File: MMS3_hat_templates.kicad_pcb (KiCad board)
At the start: 4 copper layers, 100 x 50 mm, 61 parts, among them J1 Chainbus in, J2 Chainbus Out, J3 Conn_01x04_Pin, J4 AMASS XT60 Male, J5 AMASS XT60 Female, J8 Conn_01x03_Pin, SW1 SW_DIP_x04, U2 M24C64, U3 SN74CB3Q3245PWR, U4 AMS1117, U5 LM2596HVS-ADJRG

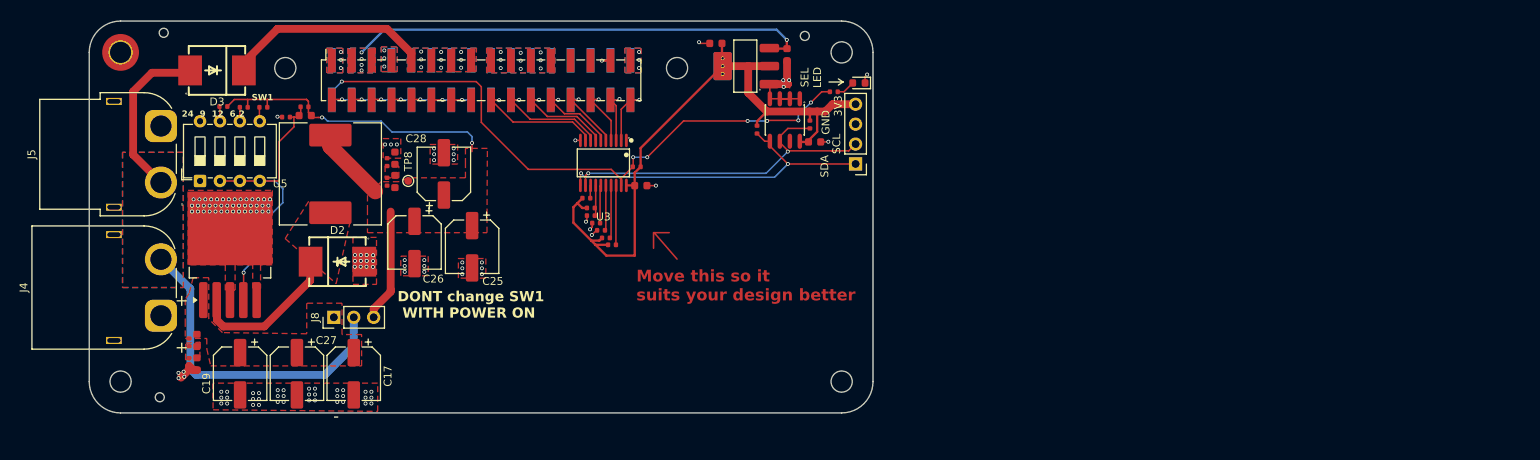
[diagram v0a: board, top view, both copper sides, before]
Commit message: ServoController
Dodano arkusz sterownika servo, aktualizacja polaczen
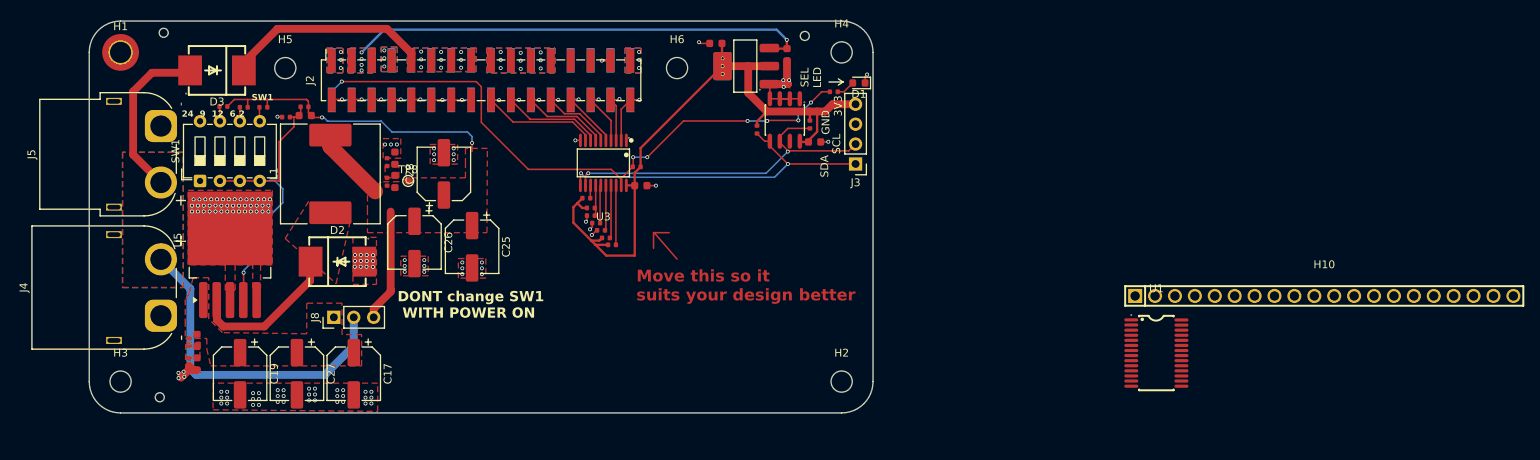
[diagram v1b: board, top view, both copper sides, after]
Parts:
- added H10: 210S-1*20P L=11.6MMGold-plated black, easyeda2kicad:HDR-TH_20P-P2.54-V-M-1, F.Cu at (235.6, 123.1)
- added U1: PCA9685PW,118, easyeda2kicad:TSSOP-28_L9.7-W4.4-P0.65-LS6.4-TL, F.Cu at (214.2, 130.4)

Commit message: updated PCB to up-to-date template:
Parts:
- removed C16, C18: 10uF, PCM_JLCPCB:C_0603
- removed C17, C19, C25, C26, C27, C28: 47u, Capacitor_SMD:CP_Elec_6.3x7.7
- removed C2, C20, C21, C23, C24: 100nF, PCM_JLCPCB:C_0603
- removed C22: 3.3nF, PCM_JLCPCB:C_0603
- removed D1: LED, LED_SMD:LED_0603_1608Metric
- removed D2, D3: SS510C, SS510C:SMC_L7.1-W6.2-LS8.1-RD
- removed H10: 210S-1*20P L=11.6MMGold-plated black, easyeda2kicad:HDR-TH_20P-P2.54-V-M-1
- removed H7, H8, H9: ~, PCM_JLCPCB:Hole_Tooling_JLCPCB
- removed L1: 100uH 4A, Inductor_SMD:L_Sunlord_SWRB1207S
- removed R12: 1kΩ, PCM_JLCPCB:R_0402
- removed R13: 18.7k, PCM_JLCPCB:R_0402
- removed R14: 16.5k, PCM_JLCPCB:R_0402
- removed R15: 9.53k, PCM_JLCPCB:R_0402
- removed R16: 5.11k, PCM_JLCPCB:R_0402
- removed R17, R18: 33kΩ, PCM_JLCPCB:R_0402
- removed R4: 10kΩ, PCM_JLCPCB:R_0402
- removed SW1: SW_DIP_x04, Button_Switch_THT:SW_DIP_SPSTx04_Slide_6.7x11.72mm_W7.62mm_P2.54mm_LowProfile
- removed TP8: TestPoint, TestPoint:TestPoint_Pad_D1.0mm
- removed U2: M24C64, PCM_JLCPCB:SOIC-8_L5.0-W4.0-P1.27-LS6.0-BL
- removed U4: AMS1117, PCM_JLCPCB:SOT-223-3_L6.5-W3.4-P2.30-LS7.0-BR
- removed U5: LM2596HVS-ADJRG, Package_TO_SOT_SMD:TO-263-5_TabPin3
- added C29: 10uF, PCM_JLCPCB:C_0603, F.Cu at (223.5, 120.6)
- added C30: 100nF, PCM_JLCPCB:C_0603, F.Cu at (223.5, 122.9)
- added D4: SS510C, SS510C:SMC_L7.1-W6.2-LS8.1-RD, F.Cu at (100.0, 101.0)
- added D5: Red, PCM_JLCPCB:D_0603, F.Cu at (176.1, 97.9)
- added D6: Red, PCM_JLCPCB:D_0603, F.Cu at (219.6, 120.8)
- added D7: Red, PCM_JLCPCB:D_0603, F.Cu at (219.6, 123.4)
- added J10: Conn_01x03, Connector_JST:JST_XH_S3B-XH-A_1x03_P2.50mm_Horizontal, F.Cu at (140.0, 132.7)
- added J11: Conn_01x03, Connector_JST:JST_XH_S3B-XH-A_1x03_P2.50mm_Horizontal, F.Cu at (161.7, 132.7)
- added J6: Conn_01x03, Connector_JST:JST_XH_S3B-XH-A_1x03_P2.50mm_Horizontal, F.Cu at (92.2, 132.7)
- added J7: Conn_01x03, Connector_JST:JST_XH_S3B-XH-A_1x03_P2.50mm_Horizontal, F.Cu at (104.2, 132.7)
- added J9: Conn_01x03, Connector_JST:JST_XH_S3B-XH-A_1x03_P2.50mm_Horizontal, F.Cu at (128.1, 132.7)
- added R21: 10kΩ, PCM_JLCPCB:R_0402, F.Cu at (200.7, 112.8)
- added R23: 10kΩ, PCM_JLCPCB:R_0402, F.Cu at (210.4, 124.1)
- added R24: 10kΩ, PCM_JLCPCB:R_0402, F.Cu at (210.4, 126.0)
- added R25: 10kΩ, PCM_JLCPCB:R_0402, F.Cu at (210.4, 127.8)
- added R26: 10kΩ, PCM_JLCPCB:R_0402, F.Cu at (213.2, 120.4)
- added R27: 10kΩ, PCM_JLCPCB:R_0402, F.Cu at (213.2, 122.3)
- added R28: 10kΩ, PCM_JLCPCB:R_0402, F.Cu at (213.2, 124.1)
- added R29: 10kΩ, PCM_JLCPCB:R_0402, F.Cu at (213.2, 126.0)
- added R30: 10kΩ, PCM_JLCPCB:R_0402, F.Cu at (213.2, 127.8)
- added R31: 10kΩ, PCM_JLCPCB:R_0402, F.Cu at (216.1, 120.4)
- added R32: 10kΩ, PCM_JLCPCB:R_0402, F.Cu at (216.1, 122.3)
- added R33: 10kΩ, PCM_JLCPCB:R_0402, F.Cu at (216.1, 124.1)
- added R34: 10kΩ, PCM_JLCPCB:R_0402, F.Cu at (216.1, 126.0)
- J8: value Conn_01x03_Pin -> Conn_01x03; footprint Connector_PinHeader_2.54mm:PinHeader_1x03_P2.54mm_Vertical -> Connector_JST:JST_XH_S3B-XH-A_1x03_P2.50mm_Horizontal
- R10, R11: value 33kΩ -> 510Ω
- moved R11 120.0 mm to (210.4, 122.3), turned to 0 degrees
- moved R10 120.0 mm to (210.4, 120.4), turned to 0 degrees
- moved U3 63.0 mm to (206.5, 108.7), turned to 0 degrees
- moved C1 60.0 mm to (208.2, 114.0)
- moved R8 59.1 mm to (200.7, 105.4)
- moved R9 59.0 mm to (200.7, 107.2), turned to 0 degrees
- moved R20 58.1 mm to (200.7, 110.9), turned to 0 degrees
- moved R19 57.7 mm to (200.7, 109.1), turned to 0 degrees
- moved R7 56.6 mm to (197.9, 114.6)
- moved R6 54.0 mm to (197.9, 112.8)
- moved R5 53.5 mm to (197.9, 110.9)
- moved R3 35.4 mm to (197.9, 109.1), turned to 0 degrees
- moved R2 28.6 mm to (197.9, 107.2), turned to 0 degrees
- moved U1 21.0 mm to (195.1, 121.6)
- moved J4 17.1 mm to (90.5, 108.8)
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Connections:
- J4 pad 2: Vin -> /Power Connector/VIN_BRD
- J5 pad 2: Vin -> /Power Connector/VIN_BRD
- J8 pad 1: Net-(J8-Pin_1) -> GND
- J8 pad 2: Vin -> /Servo controller/S3
- J8 pad 3: U_reg -> /Power Connector/VIN_BRD
- R10 pad 1: Net-(J8-Pin_1) -> /Servo controller/S16
- R10 pad 2: Net-(C20-Pad2) -> Net-(D7-Pad2)
- R11 pad 1: Net-(C20-Pad2) -> /Servo controller/S15
- R11 pad 2: GND -> Net-(D6-Pad2)
- R19 pad 1: /Bus_switch/Chainbus.MISO -> +3V3
- R19 pad 2: GND -> /Bus_switch/Chainbus.SDA
- R2 pad 2: /Bus_switch/Chainbus.SCL -> /Bus_switch/Chainbus.CS
- R3 pad 2: /Bus_switch/Chainbus.SDA -> /Bus_switch/Chainbus.SCK
- R5 pad 1: +3V3 -> /Bus_switch/Chainbus.SCK
- R5 pad 2: /Bus_switch/Chainbus.RX -> GND
- R6 pad 2: /Bus_switch/Chainbus.TX -> /Bus_switch/Chainbus.SCL
- R7 pad 2: /Bus_switch/Chainbus.CS -> /Bus_switch/Chainbus.TX
- R8 pad 2: /Bus_switch/Chainbus.SCK -> /Bus_switch/Chainbus.RX
- R9 pad 1: /Bus_switch/Chainbus.SCK -> /Bus_switch/Chainbus.MISO
- U1 pad 1: GND -> /Servo controller/A0
- U1 pad 10: unconnected-(U1-LED4-Pad10) -> /Servo controller/S5
- U1 pad 11: unconnected-(U1-LED5-Pad11) -> /Servo controller/S6
- U1 pad 17: Net-(U1-LED10) -> unconnected-(U1-LED10-Pad17)
- U1 pad 18: Net-(U1-LED11) -> unconnected-(U1-LED11-Pad18)
- U1 pad 19: Net-(U1-LED12) -> unconnected-(U1-LED12-Pad19)
- U1 pad 2: GND -> /Servo controller/A1
- U1 pad 20: Net-(U1-LED13) -> unconnected-(U1-LED13-Pad20)
- U1 pad 21: Net-(U1-LED14) -> /Servo controller/S15
- U1 pad 22: Net-(U1-LED15) -> /Servo controller/S16
- U1 pad 23: unconnected-(U1-~{OE}-Pad23) -> GND
- U1 pad 24: GND -> /Servo controller/A5
- U1 pad 28: +5V -> +3V3
- U1 pad 3: GND -> /Servo controller/A2
- U1 pad 4: GND -> /Servo controller/A3
- U1 pad 5: GND -> /Servo controller/A4
- U1 pad 6: unconnected-(U1-LED0-Pad6) -> /Servo controller/S1
- U1 pad 7: unconnected-(U1-LED1-Pad7) -> /Servo controller/S2
- U1 pad 8: unconnected-(U1-LED2-Pad8) -> /Servo controller/S3
- U1 pad 9: unconnected-(U1-LED3-Pad9) -> /Servo controller/S4
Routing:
- net +3V3: track 83.4 -> 0.00 mm
- net /Bus_switch/SEL1: track 80.3 -> 0.00 mm, vias 7 -> 0
- net Vin: track 64.7 -> 0.00 mm
- net U_reg: track 62.3 -> 0.00 mm, vias 2 -> 0
- net +5V: track 59.4 -> 0.00 mm, vias 5 -> 3
- net /Bus_switch/Chainbus.SCL: track 43.9 -> 0.00 mm, vias 2 -> 0
- net /Bus_switch/Chainbus.SDA: track 43.4 -> 0.00 mm, vias 2 -> 0
- net Net-(U5-FB): track 38.1 -> 0.00 mm, vias 1 -> 0
- net BRD_VIN: track 25.9 -> 0.00 mm, vias 9 -> 6
- net GND: track 25.7 -> 0.00 mm, vias 145 -> 21
- net Net-(D2-K): track 21.4 -> 0.00 mm
- net /Bus_switch/Chainbus_In.SDA: track 16.7 -> 2.09 mm
- net /Bus_switch/Chainbus_In.SCL: track 14.8 -> 2.11 mm
- net /Bus_switch/Chainbus_In.CS: track 12.9 -> 2.13 mm
- net /Bus_switch/Chainbus_In.SCK: track 10.9 -> 1.95 mm
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- added copper zone on F.Cu, net /Power Connector/VIN_BRD
- removed copper zone on In1.Cu, net GND
- removed copper zone on In2.Cu, net GND
- removed copper zone on F.Cu, net Net-(C20-Pad2)
- removed copper zone on F.Cu, net Net-(C23-Pad2)
- removed copper zone on F.Cu, net Net-(D2-K)
- removed copper zone on F.Cu, net Net-(J8-Pin_1)
- removed copper zone on F.Cu, net U_reg
- removed copper zone on B.Cu, net Vin
- removed copper zone on F.Cu, net Vin
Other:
- copper layers 4 -> 2
- board text removed: "24 9 12 6.2"
- board text removed: "DONT change SW1 WITH POWER ON"
- board text removed: "Move this so it suits your design better"
- board text removed: "SW1"
